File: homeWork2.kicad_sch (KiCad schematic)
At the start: 54 parts, among them J1 Barrel_Jack_Switch_SMT, J2 Conn_01x15_Socket, J3 Conn_01x15_Socket, J4_LCD1 Conn_01x04_Socket_LCD, J5_DFPLAYER1 Conn_01x04_Socket_DFPLAYER, U1 LM7805_TO220

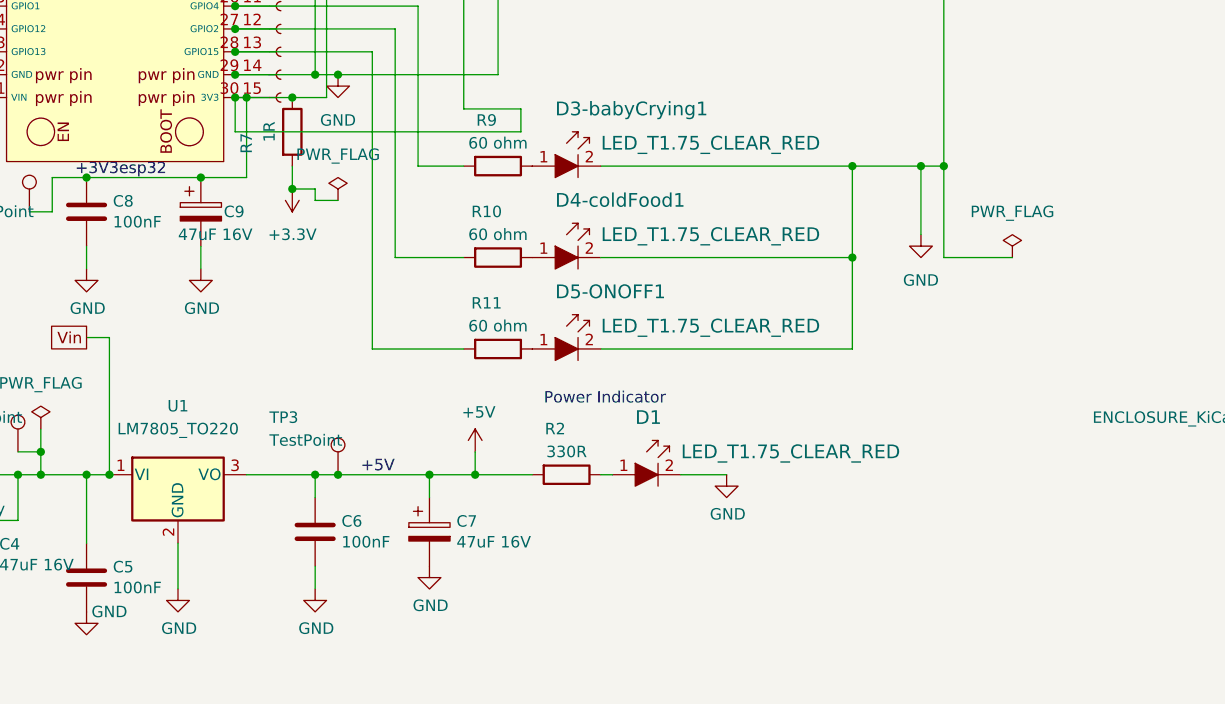
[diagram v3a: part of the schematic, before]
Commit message: PCB and schematics edits. Added a connector for the UART interface and a connection for the I2C interface.
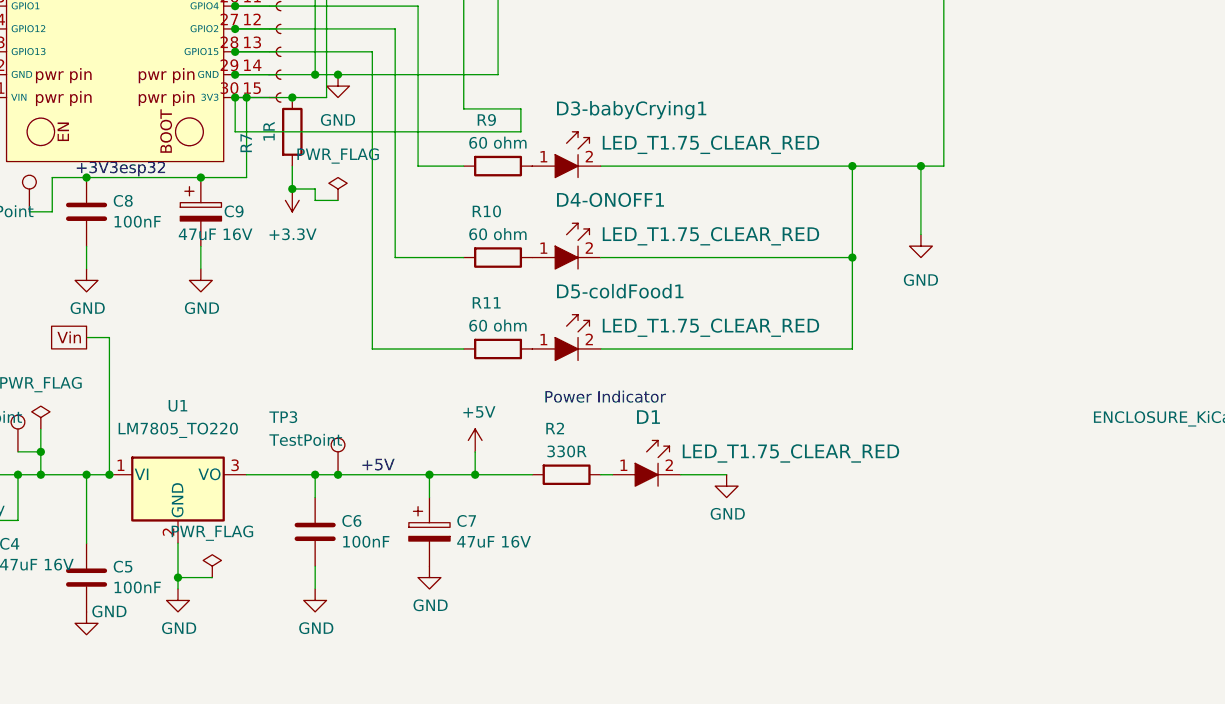
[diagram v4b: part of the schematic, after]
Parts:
- renumbered D4-coldFood1 to D4-ONOFF1, D5-ONOFF1 to D5-coldFood1
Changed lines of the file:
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@@
   (junction (at 121.92 125.73) (diameter 0) (color 0 0 0 0)
   )
+  (junction (at 119.38 170.18) (diameter 0) (color 0 0 0 0)
+  )
   (junction (at 152.4 158.75) (diameter 0) (color 0 0 0 0)
   )
@@
   (junction (at 57.15 107.95) (diameter 0) (color 0 0 0 0)
   )
-  (junction (at 204.47 124.46) (diameter 0) (color 0 0 0 0)
-  )
   (wire (pts (xy 254 96.52) (xy 246.38 96.52))
     (stroke (width 0) (type default))
@@
     (stroke (width 0) (type default))
   )
-  (wire (pts (xy 119.38 171.45) (xy 119.38 166.37))
+  (wire (pts (xy 119.38 166.37) (xy 119.38 170.18))
     (stroke (width 0) (type default))
   )
@@
     (stroke (width 0) (type default))
   )
-  (wire (pts (xy 204.47 134.62) (xy 204.47 124.46))
-    (stroke (width 0) (type default))
-  )
   (wire (pts (xy 67.31 74.93) (xy 67.31 77.47))
     (stroke (width 0) (type default))
@@
     (stroke (width 0) (type default))
   )
+  (wire (pts (xy 123.19 170.18) (xy 119.38 170.18))
+    (stroke (width 0) (type default))
+  )
   (wire (pts (xy 246.38 96.52) (xy 246.38 104.14))
     (stroke (width 0) (type default))
@@
     (stroke (width 0) (type default))
   )
+  (wire (pts (xy 119.38 170.18) (xy 119.38 171.45))
+    (stroke (width 0) (type default))
+  )
   (wire (pts (xy 81.28 166.37) (xy 81.28 161.29))
     (stroke (width 0) (type default))
@@
     (stroke (width 0) (type default))
   )
-  (wire (pts (xy 212.09 134.62) (xy 204.47 134.62))
-    (stroke (width 0) (type default))
-  )
   (wire (pts (xy 81.28 158.75) (xy 78.74 158.75))
     (stroke (width 0) (type default))
@@
   (symbol (lib_id "GPAD_SCH_LIB:LED_T1.75_CLEAR_WHITE") (at 163.83 134.62 0) (unit 1)
     (in_bom yes) (on_board yes) (dnp no)
-    (property "Reference" "D4-coldFood1" (at 161.29 128.27 0)
+    (property "Reference" "D4-ONOFF1" (at 161.29 128.27 0)
       (effects (font (size 1.524 1.524)) (justify left))
     )
@@
       (project "homeWork2"
         (path "/0dd285f0-5d03-432a-a2cf-fee3b00868c5"
-          (reference "D4-coldFood1") (unit 1)
+          (reference "D4-ONOFF1") (unit 1)
         )
       )
@@
   (symbol (lib_id "GPAD_SCH_LIB:LED_T1.75_CLEAR_WHITE") (at 163.83 144.78 0) (unit 1)
     (in_bom yes) (on_board yes) (dnp no)
-    (property "Reference" "D5-ONOFF1" (at 161.29 138.43 0)
+    (property "Reference" "D5-coldFood1" (at 161.29 138.43 0)
       (effects (font (size 1.524 1.524)) (justify left))
     )
@@
       (project "homeWork2"
         (path "/0dd285f0-5d03-432a-a2cf-fee3b00868c5"
-          (reference "D5-ONOFF1") (unit 1)
+          (reference "D5-coldFood1") (unit 1)
         )
       )
@@
     )
   )
+  (symbol (lib_id "power:PWR_FLAG") (at 123.19 170.18 0) (unit 1)
+    (in_bom yes) (on_board yes) (dnp no)
+    (property "Reference" "#FLG01" (at 123.19 168.275 0)
+      (effects (font (size 1.27 1.27)) hide)
+    )
+    (property "Value" "PWR_FLAG" (at 123.19 165.1 0)
+      (effects (font (size 1.27 1.27)))
+    )
+    (property "Footprint" "" (at 123.19 170.18 0)
+      (effects (font (size 1.27 1.27)) hide)
+    )
+    (property "Datasheet" "~" (at 123.19 170.18 0)
+      (effects (font (size 1.27 1.27)) hide)
+    )
+    (pin "1")
+    (instances
+      (project "homeWork2"
+        (path "/0dd285f0-5d03-432a-a2cf-fee3b00868c5"
+          (reference "#FLG01") (unit 1)
+        )
+      )
+      (project "GeneralPurposeAlarmDevicePCB"
+        (path "/412a327d-1ee3-473e-bc00-1545004b7edf"
+          (reference "#FLG0102") (unit 1)
+        )
+      )
+    )
+  )
   (symbol (lib_id "Device:R") (at 154.94 124.46 270) (unit 1)
     (in_bom yes) (on_board yes) (dnp no)
@@
         )
       )
-    )
-  )
-  (symbol (lib_id "power:PWR_FLAG") (at 212.09 134.62 0) (unit 1)
-    (in_bom yes) (on_board yes) (dnp no) (fields_autoplaced)
-    (property "Reference" "#FLG0109" (at 212.09 132.715 0)
-      (effects (font (size 1.27 1.27)) hide)
-    )
-    (property "Value" "PWR_FLAG" (at 212.09 129.54 0)
-      (effects (font (size 1.27 1.27)))
-    )
-    (property "Footprint" "" (at 212.09 134.62 0)
-      (effects (font (size 1.27 1.27)) hide)
-    )
-    (property "Datasheet" "~" (at 212.09 134.62 0)
-      (effects (font (size 1.27 1.27)) hide)
-    )
-    (pin "1")
-    (instances
-      (project "homeWork2"
-        (path "/0dd285f0-5d03-432a-a2cf-fee3b00868c5"
-          (reference "#FLG0109") (unit 1)
-        )
-      )

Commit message: migrated the library, and updated the symbols in the schematic from the migrated library.
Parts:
- D1: DK_Detail_Page /product-detail/en/lite-on-inc/LTL2R3KEK/160-1682-ND/573572 -> /product-detail/en/lite-on-inc/LTW-2R3D7/160-1772-ND/1277121; Digi-Key_PN 160-1682-ND -> 160-1772-ND; MPN (none) -> LTW-2R3D7
- D3-babyCrying1, D4-ONOFF1, D5-coldFood1, D6-lostSock1, D7-unstableGround1, D8-highBloodPreasure1, D9-MUTE1: footprint PubInv_KiCad_PCB:LED_5mm_Radial -> GeneralPurposeAlarmDevicePCB:LED_5mm_Radial; DK_Detail_Page /product-detail/en/lite-on-inc/LTL2R3KEK/160-1682-ND/573572 -> /product-detail/en/lite-on-inc/LTW-2R3D7/160-1772-ND/1277121; Digi-Key_PN 160-1682-ND -> 160-1772-ND; MPN (none) -> LTW-2R3D7
- ESP32_DEVKITV1: footprint PubInv_KiCad_PCB:ESP32_DEVKITV1 -> esp32 15 pin Library:esp32
- H1, H2, H3, H4: footprint PubInv_KiCad_PCB:MountingHole_3.5mm_Pad_Via -> GeneralPurposeAlarmDevicePCB:MountingHole_3.5mm_Pad_Via
- J1: footprint PubInv_KiCad_PCB:BarrelJack_CLIFF_FC681465S_SMT_Horizontal -> GeneralPurposeAlarmDevicePCB:BarrelJack_CLIFF_FC681465S_SMT_Horizontal; Manufacturier (none) -> XKB Connectivity / Tensility International Corp
- S1-morseCodeDanger1, S2-RepeatCalculation1, S3-muteFiveMin1, S4-SendEmergMessage1: footprint PubInv_KiCad_PCB:Switch_Tactile_THT_6x6mm -> GeneralPurposeAlarmDevicePCB:Switch_Tactile_THT_6x6mm; Assembly Type (none) -> HAND

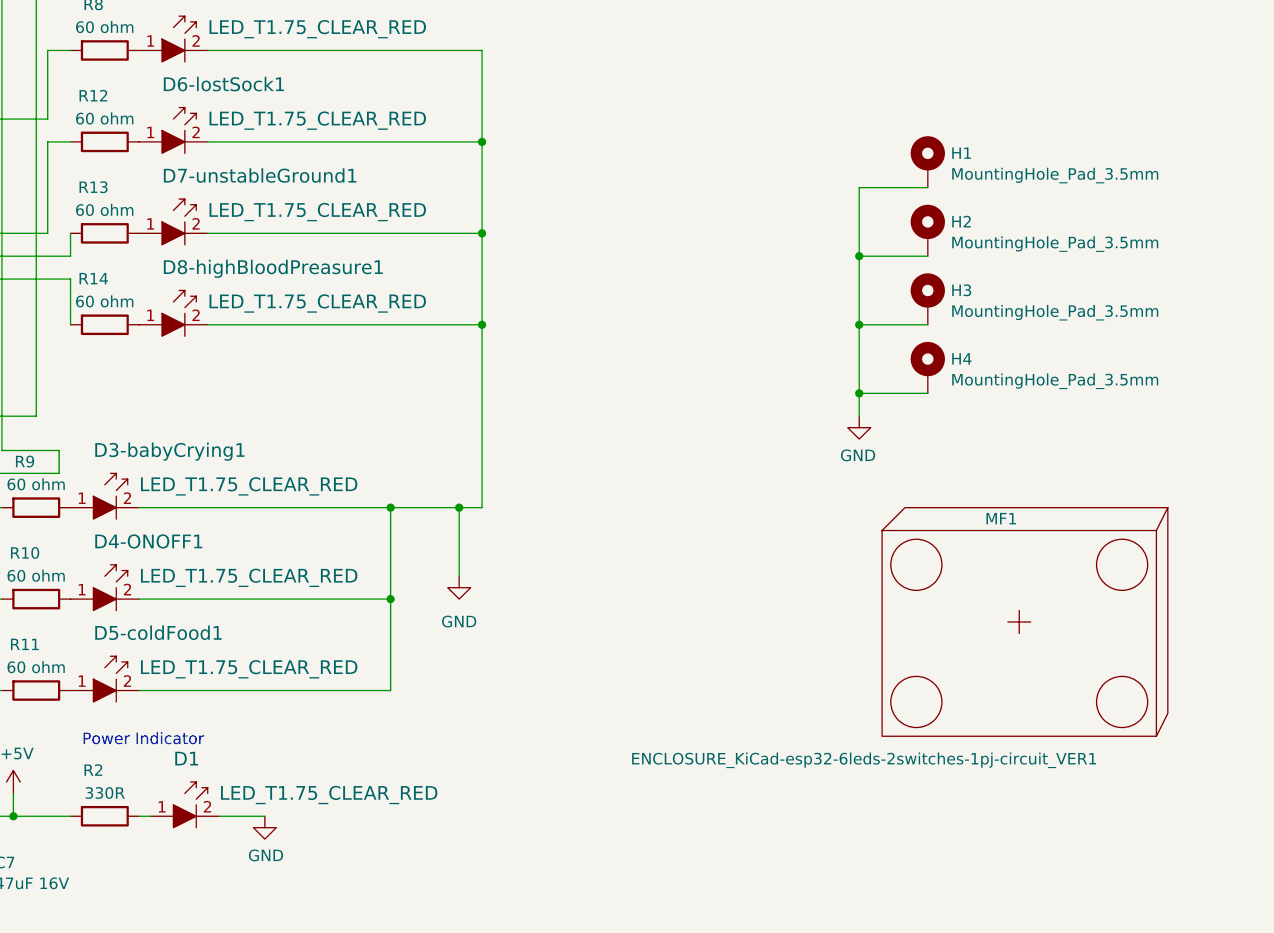
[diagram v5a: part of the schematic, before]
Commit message: Cleared the ERC errors.
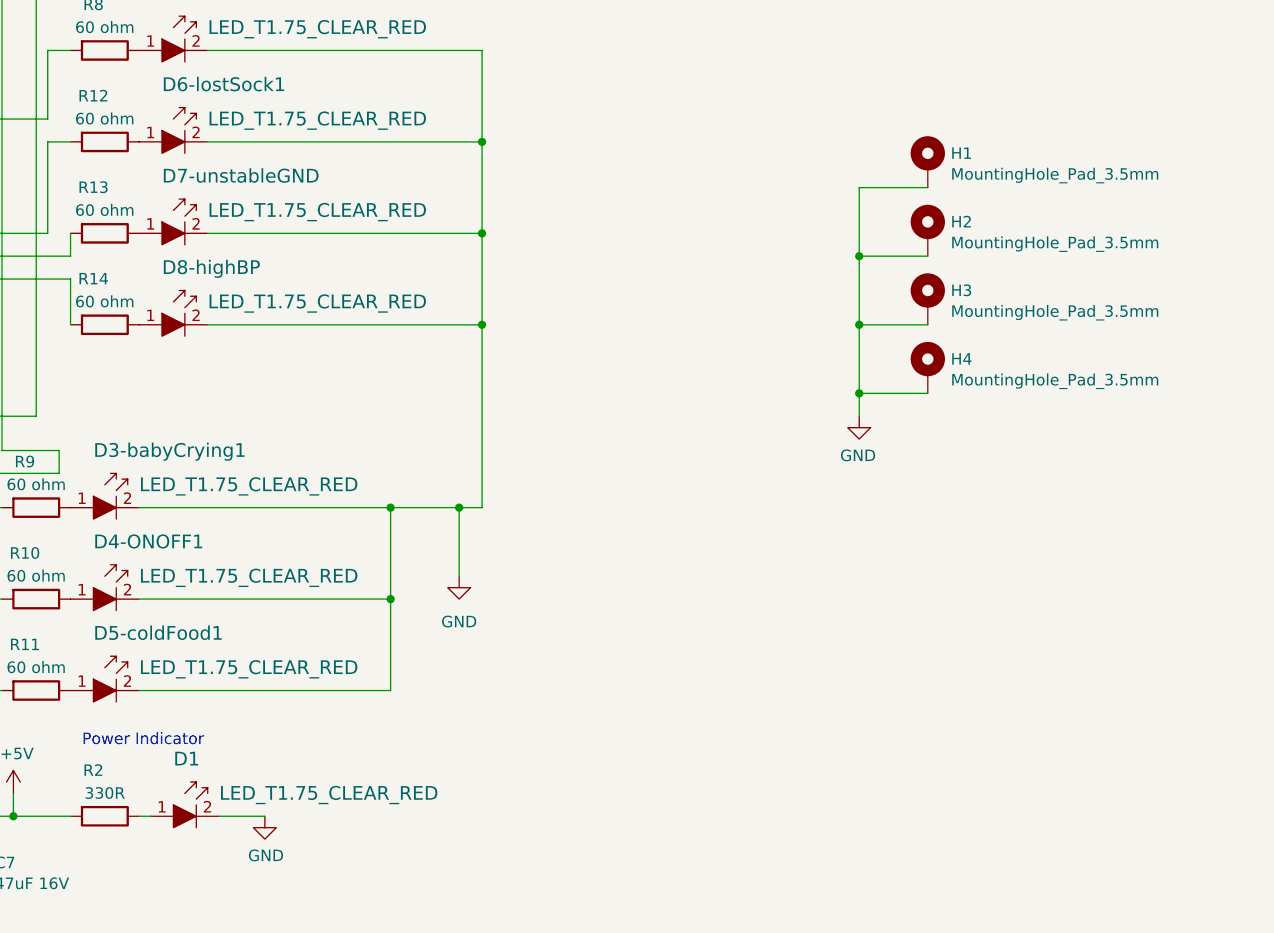
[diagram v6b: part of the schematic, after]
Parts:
- removed MF1: ENCLOSURE_KiCad-esp32-6leds-2switches-1pj-circuit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, symbol GPAD_SCH_LIB:ENCLOSURE_GPAD_VER1
- renumbered D7-unstableGround1 to D7-unstableGND, D8-highBloodPreasure1 to D8-highBP
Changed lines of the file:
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@@
   (symbol (lib_id "GPAD_SCH_LIB:LED_T1.75_CLEAR_WHITE") (at 171.45 93.98 0) (unit 1)
     (in_bom yes) (on_board yes) (dnp no)
-    (property "Reference" "D7-unstableGround1" (at 168.91 87.63 0)
+    (property "Reference" "D7-unstableGND" (at 168.91 87.63 0)
       (effects (font (size 1.524 1.524)) (justify left))
     )
@@
       (project "homeWork2"
         (path "/0dd285f0-5d03-432a-a2cf-fee3b00868c5"
-          (reference "D7-unstableGround1") (unit 1)
+          (reference "D7-unstableGND") (unit 1)
         )
       )
@@
   )
   (symbol (lib_id "PubInv_KiCad_SCH_LIB:ESP32_DEVKITV1") (at 100.33 73.66 0) (unit 1)
-    (in_bom yes) (on_board yes) (dnp no) (fields_autoplaced)
+    (in_bom yes) (on_board no) (dnp no) (fields_autoplaced)
     (property "Reference" "ESP32_DEVKITV1" (at 112.395 71.12 0)
       (effects (font (size 1.27 1.27)))
@@
     )
   )
-  (symbol (lib_id "GPAD_SCH_LIB:ENCLOSURE_GPAD_VER1") (at 264.16 137.16 0) (unit 1)
-    (in_bom yes) (on_board no) (dnp no)
-    (property "Reference" "MF1" (at 260.35 125.73 0)
-      (effects (font (size 1.27 1.27)) (justify left))
-    )
-    (property "Value" "ENCLOSURE_KiCad-esp32-6leds-2switches-1pj-circuit_VER1" (at 220.98 152.4 0)
-      (effects (font (size 1.27 1.27)) (justify left))
-    )
-    (property "Footprint" "" (at 264.16 137.16 0)
-      (effects (font (size 1.27 1.27)) hide)
-    )
-    (property "Datasheet" "" (at 264.16 137.16 0)
-      (effects (font (size 1.27 1.27)) hide)
-    )
-    (property "Distributor 1" "Nagham" (at 264.16 137.16 0)
-      (effects (font (size 1.27 1.27)) hide)
-    )
-    (property "Distributor 1 PN" "ENCLOSURE_KiCad-esp32-6leds-2switches-1pj-circuit_VER1" (at 264.16 137.16 0)
-      (effects (font (size 1.27 1.27)) hide)
-    )
-    (property "Cost" "1000000" (at 264.16 137.16 0)
-      (effects (font (size 1.27 1.27)) hide)
-    )
-    (property "Distributor 2" "" (at 264.16 137.16 0)
-      (effects (font (size 1.27 1.27)) hide)
-    )
-    (property "Distributor 2 PN" "" (at 264.16 137.16 0)
-      (effects (font (size 1.27 1.27)) hide)
-    )
-    (instances
-      (project "homeWork2"
-        (path "/0dd285f0-5d03-432a-a2cf-fee3b00868c5"
-          (reference "MF1") (unit 1)
-        )
-      )
-      (project "GeneralPurposeAlarmDevicePCB"
-        (path "/412a327d-1ee3-473e-bc00-1545004b7edf"
-          (reference "MF102") (unit 1)
-        )
-      )
-    )
-  )
   (symbol (lib_id "power:GND") (at 76.2 176.53 0) (unit 1)
     (in_bom yes) (on_board yes) (dnp no)
@@
   (symbol (lib_id "GPAD_SCH_LIB:LED_T1.75_CLEAR_WHITE") (at 171.45 104.14 0) (unit 1)
     (in_bom yes) (on_board yes) (dnp no)
-    (property "Reference" "D8-highBloodPreasure1" (at 168.91 97.79 0)
+    (property "Reference" "D8-highBP" (at 168.91 97.79 0)
       (effects (font (size 1.524 1.524)) (justify left))
     )
@@
       (project "homeWork2"
         (path "/0dd285f0-5d03-432a-a2cf-fee3b00868c5"
-          (reference "D8-highBloodPreasure1") (unit 1)
-        )
-      )
+          (reference "D8-highBP") (unit 1)
+        )
+      )

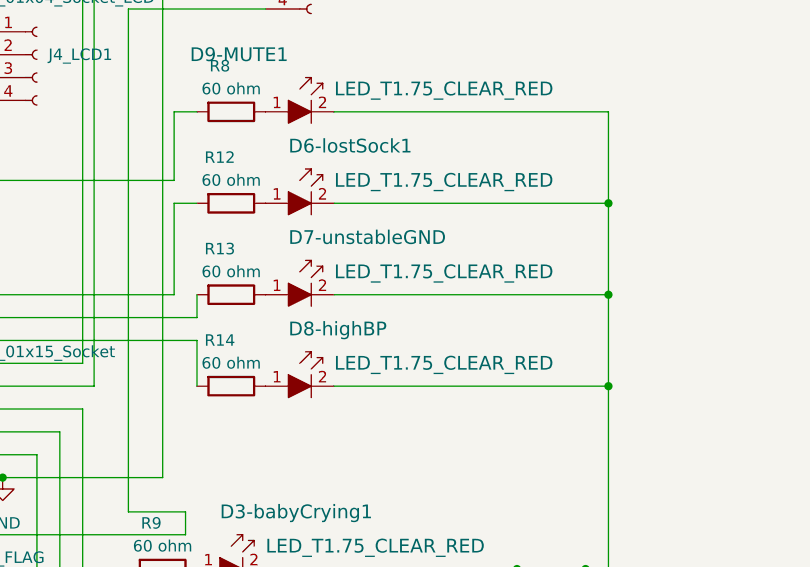
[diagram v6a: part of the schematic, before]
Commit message: Cleared the DRC ERRORS.
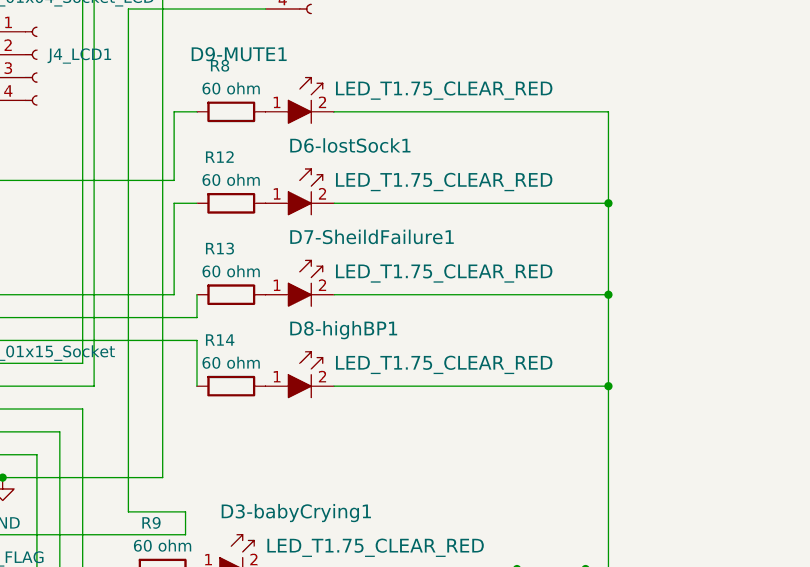
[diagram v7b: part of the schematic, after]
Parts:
- renumbered D7-unstableGND to D7-SheildFailure1, D8-highBP to D8-highBP1
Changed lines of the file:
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@@
   (symbol (lib_id "GPAD_SCH_LIB:LED_T1.75_CLEAR_WHITE") (at 171.45 93.98 0) (unit 1)
     (in_bom yes) (on_board yes) (dnp no)
-    (property "Reference" "D7-unstableGND" (at 168.91 87.63 0)
+    (property "Reference" "D7-SheildFailure1" (at 168.91 87.63 0)
       (effects (font (size 1.524 1.524)) (justify left))
     )
@@
       (project "homeWork2"
         (path "/0dd285f0-5d03-432a-a2cf-fee3b00868c5"
-          (reference "D7-unstableGND") (unit 1)
+          (reference "D7-SheildFailure1") (unit 1)
         )
       )
@@
   (symbol (lib_id "GPAD_SCH_LIB:LED_T1.75_CLEAR_WHITE") (at 171.45 104.14 0) (unit 1)
     (in_bom yes) (on_board yes) (dnp no)
-    (property "Reference" "D8-highBP" (at 168.91 97.79 0)
+    (property "Reference" "D8-highBP1" (at 168.91 97.79 0)
       (effects (font (size 1.524 1.524)) (justify left))
     )
@@
       (project "homeWork2"
         (path "/0dd285f0-5d03-432a-a2cf-fee3b00868c5"
-          (reference "D8-highBP") (unit 1)
-        )
-      )
+          (reference "D8-highBP1") (unit 1)
+        )
+      )
